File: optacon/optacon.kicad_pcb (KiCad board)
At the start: 2 copper layers, 41.1 x 28.6 mm, 9 parts, among them J1 Conn_01x22, J2 Conn_01x08, J3 Conn_01x02, U1 HV528, U2 HV528

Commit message: schematic, footprints
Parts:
- added C1: 1 µF, Capacitor_SMD:C_0805_2012Metric, F.Cu at (157.4, 88.8)
- added C2: 0.1 µF, Capacitor_SMD:C_0805_2012Metric, F.Cu at (151.7, 92.1)
- added C3: 0.1 µF, Capacitor_SMD:C_0805_2012Metric, F.Cu at (162.9, 82.5)
- added C4: 0.1 µF 150V+, Capacitor_SMD:C_1206_3216Metric, F.Cu at (152.3, 89.0)
- added D1: D, Diode_SMD:D_0805_2012Metric, F.Cu at (91.9, 125.6)
- added L1: 3.3 µH, microchip_hv:TDK_VLS_3012, F.Cu at (158.2, 83.6)
- added R1: 549k, Resistor_SMD:R_0805_2012Metric, F.Cu at (151.7, 95.1)
- added R2: 6.98k, Resistor_SMD:R_0805_2012Metric, F.Cu at (162.9, 85.5)
- added R3: 6.98k, Resistor_SMD:R_0805_2012Metric, F.Cu at (161.8, 88.4)
- added R4: 3.3k, Resistor_SMD:R_0805_2012Metric, F.Cu at (151.7, 98.1)
- added R5: 3.3k, Resistor_SMD:R_0805_2012Metric, F.Cu at (156.2, 92.1)
- added U3: DRV2665, Package_DFN_QFN:Texas_S-PVQFN-N20_EP2.7x2.7mm_ThermalVias, F.Cu at (152.7, 84.1)
- added piezo1: Conn_01x21, microchip_hv:piezox20, F.Cu at (104.0, 83.5)
- J1: value Conn_01x22 -> Conn_01x12; footprint microchip_hv:piezox20 -> microchip_hv:FH34SRJ-12S-0.5SH
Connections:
- J1 pad 1: /reed1 -> /VDD
- J1 pad 10: /reed10 -> /SCL
- J1 pad 11: /reed11 -> /SDA
- J1 pad 12: /reed12 -> /REG
- J1 pad 2: /reed2 -> /VBIAS
- J1 pad 3: /reed3 -> /DIN
- J1 pad 4: /reed4 -> /CLK
- J1 pad 5: /reed5 -> /POL
- J1 pad 6: /reed6 -> /LE
- J1 pad 7: /reed7 -> /DOUT
- J1 pad 8: /reed8 -> GND
- J1 pad 9: /reed9 -> /IN+
- U1 pad 10: /PZT+ -> /PZT_Common
- U1 pad 11: /PZT+ -> /PZT_Common
- U1 pad 12: /PZT+ -> /PZT_Common
- U1 pad 29: /PZT- -> /PZT_Common
- U1 pad 30: /PZT- -> /PZT_Common
- U1 pad 31: /PZT- -> /PZT_Common
- U2 pad 10: /PZT+ -> /PZT_Common
- U2 pad 11: /PZT+ -> /PZT_Common
- U2 pad 12: /PZT+ -> /PZT_Common
- U2 pad 29: /PZT- -> /PZT_Common
- U2 pad 30: /PZT- -> /PZT_Common
- U2 pad 31: /PZT- -> /PZT_Common
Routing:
- net /PZT_Common: track 0.00 -> 116.4 mm, vias 0 -> 28
- net /PZT+: track 66.9 -> 0.00 mm, vias 23 -> 0
- net /PZT-: track 49.5 -> 0.00 mm, vias 5 -> 0
- net /reed11: track 10.1 -> 0.00 mm, vias 1 -> 0
- net /POL: track 19.8 -> 29.9 mm, vias 3 -> 4
- net GND: track 8.66 -> 17.9 mm, vias 3 -> 4
- net /reed10: track 9.23 -> 0.00 mm, vias 1 -> 0
- net /reed9: track 8.81 -> 0.00 mm, vias 1 -> 0
- net /SCL: track 0.00 -> 8.81 mm, vias 0 -> 1
- net /reed13: track 8.60 -> 0.00 mm, vias 1 -> 0
- net /VDD: track 27.5 -> 36.1 mm, vias 2 -> 3
- net /reed12: track 8.16 -> 0.00 mm, vias 1 -> 0
- net /DIN: track 9.28 -> 17.4 mm, vias 0 -> 1
- net /reed8: track 7.96 -> 0.00 mm, vias 1 -> 0
- net /SDA: track 0.00 -> 7.96 mm, vias 0 -> 1

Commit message: bom update
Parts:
- removed J2: Conn_01x08, Connector_PinHeader_2.54mm:PinHeader_1x08_P2.54mm_Vertical
- removed J3: Conn_01x02, Connector_PinHeader_2.54mm:PinHeader_1x02_P2.54mm_Vertical
- removed REF** (x4): MountingHole_2.2mm_M2_ISO7380, MountingHole:MountingHole_2.2mm_M2_ISO7380
- C1, C2, C3: footprint Capacitor_SMD:C_0805_2012Metric -> Capacitor_SMD:C_0603_1608Metric
- D1: footprint Diode_SMD:D_0805_2012Metric -> Diode_SMD:D_SOD-123F
- R1, R2, R3, R4, R5: footprint Resistor_SMD:R_0805_2012Metric -> Resistor_SMD:R_0603_1608Metric
- moved R2 68.5 mm to (98.0, 63.4), turned to -90 degrees
- moved R1 60.9 mm to (99.7, 63.4), turned to -90 degrees
- moved D1 58.1 mm to (98.4, 67.9), turned to 90 degrees
- moved C4 52.6 mm to (103.7, 68.9), turned to 180 degrees
- moved U3 52.4 mm to (104.2, 64.3)
- moved L1 49.1 mm to (113.0, 64.4)
- moved J1 31.7 mm to (103.0, 52.8), turned to 180 degrees
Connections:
- J1 pad 10: /SCL -> /REG
- J1 pad 11: /SDA -> /AIN
- J1 pad 12: /REG -> GND
- J1 pad 8: GND -> /SCL
- J1 pad 9: /IN+ -> /SDA
- U1 pad 1: /reed2 -> /PZT_Common
- U1 pad 10: /PZT_Common -> /reed8
- U1 pad 11: /PZT_Common -> /reed9
- U1 pad 12: /PZT_Common -> /reed10
- U1 pad 2: /reed3 -> /PZT_Common
- U1 pad 3: /reed4 -> /reed1
- U1 pad 32: /reed1 -> /PZT_Common
- U1 pad 4: /reed5 -> /reed2
- U1 pad 5: /reed6 -> /reed3
- U1 pad 6: /reed7 -> /reed4
- U1 pad 7: /reed8 -> /reed5
- U1 pad 8: /reed9 -> /reed6
- U1 pad 9: /reed10 -> /reed7
- U2 pad 1: /reed12 -> /reed15
- U2 pad 2: /reed13 -> /reed16
- U2 pad 29: /PZT_Common -> /reed11
- U2 pad 3: /reed14 -> /reed17
- U2 pad 30: /PZT_Common -> /reed12
- U2 pad 31: /PZT_Common -> /reed13
- U2 pad 32: /reed11 -> /reed14
- U2 pad 4: /reed15 -> /reed18
- U2 pad 5: /reed16 -> /reed19
- U2 pad 6: /reed17 -> /reed20
- U2 pad 7: /reed18 -> /PZT_Common
- U2 pad 8: /reed19 -> /PZT_Common
- U2 pad 9: /reed20 -> /PZT_Common
- U3 pad 17: /IN+ -> /AIN
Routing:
- net /PZT_Common: track 116.4 -> 0.00 mm, vias 28 -> 0
- net /VDD: track 36.1 -> 0.00 mm, vias 3 -> 0
- net /VPP: track 32.4 -> 0.00 mm, vias 2 -> 0
- net /POL: track 29.9 -> 0.00 mm, vias 4 -> 0
- net /VBIAS: track 22.3 -> 0.00 mm, vias 2 -> 0
- net /CLK: track 22.0 -> 0.00 mm, vias 3 -> 0
- net Net-(U1-Pad24): track 20.8 -> 0.00 mm, vias 2 -> 0
- net /LE: track 20.2 -> 0.00 mm, vias 2 -> 0
- net GND: track 17.9 -> 0.00 mm, vias 4 -> 0
- net /DIN: track 17.4 -> 0.00 mm, vias 1 -> 0
- net /reed1: track 9.98 -> 0.00 mm, vias 1 -> 0
- net /reed20: track 9.44 -> 0.00 mm, vias 1 -> 0
- net /SCL: track 8.81 -> 0.00 mm, vias 1 -> 0
- net /reed19: track 8.74 -> 0.00 mm, vias 1 -> 0
- net /reed3: track 8.53 -> 0.00 mm, vias 1 -> 0
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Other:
- board size 41.1 x 28.6 mm -> 124.1 x 73.2 mm
- board text added: "V-SCORE"
- board text removed: "CLK"
- board text removed: "DIN"
- board text removed: "DO"
- board text removed: "GND"
- board text removed: "LE"
- board text removed: "POL"
- board text removed: "VBS"
- board text removed: "VDD"
- board text removed: "VPP"

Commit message: driver board
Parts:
- added C5: 0.1µF, Capacitor_SMD:C_1206_3216Metric, F.Cu at (116.9, 70.9)
- added R6: 0, Resistor_SMD:R_0603_1608Metric, F.Cu at (97.6, 54.3)
- added R7: 0R, Resistor_SMD:R_1206_3216Metric, F.Cu at (120.5, 63.9)
- added R8: DNP, Resistor_SMD:R_1206_3216Metric, F.Cu at (115.4, 63.9)
- L1: value 3.3 µH -> VLS3012HBX-3R3M
- moved R4 71.0 mm to (93.3, 57.8), turned to 180 degrees
- moved R5 70.7 mm to (93.3, 59.7)
- moved C3 67.0 mm to (102.1, 54.3), turned to 180 degrees
- moved C2 62.9 mm to (100.3, 55.9), turned to 180 degrees
- moved R3 62.3 mm to (109.5, 54.7), turned to 90 degrees
- moved C1 60.7 mm to (102.4, 63.0), turned to 90 degrees
- moved J1 13.0 mm to (90.0, 53.4)
- moved C4 10.6 mm to (109.6, 60.1), turned to -90 degrees
- moved D1 9.17 mm to (104.2, 75.0)
- moved L1 7.83 mm to (105.4, 62.8), turned to 90 degrees
- moved U3 6.27 mm to (104.9, 58.1)
- moved R2 3.35 mm to (97.3, 60.1)
- moved R1 2.51 mm to (97.3, 64.1), turned to 90 degrees
- moved U1 0.76 mm to (98.3, 74.0), turned to 45 degrees
- moved U2 0.68 mm to (109.9, 74.0), turned to 135 degrees
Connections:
- net Net-(C4-Pad1) renamed /VBST
- C3 pad 1: /REG -> Net-(C3-Pad1)
- J1 pad 1: /VDD -> GND
- J1 pad 10: /REG -> /SDA
- J1 pad 11: /AIN -> /REG
- J1 pad 12: GND -> /VDD
- J1 pad 3: /DIN -> /DOUT
- J1 pad 4: /CLK -> /LE
- J1 pad 6: /LE -> /CLK
- J1 pad 7: /DOUT -> /DIN
- J1 pad 8: /SCL -> /AIN
- J1 pad 9: /SDA -> /SCL
- U1 pad 17: /DIN -> Net-(U2-Pad24)
- U1 pad 24: Net-(U1-Pad24) -> /DOUT
- U2 pad 17: Net-(U1-Pad24) -> /DIN
- U2 pad 24: /DOUT -> Net-(U2-Pad24)
- U3 pad 13: /VPP -> /VOUT
- U3 pad 16: /hv_driver/IN- -> GND
- U3 pad 20: /REG -> Net-(C3-Pad1)
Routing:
- net /PZT_Common: track 0.00 -> 63.1 mm
- net /VDD: track 0.00 -> 49.9 mm, vias 0 -> 4
- net /CLK: track 0.00 -> 38.3 mm, vias 0 -> 2
- net /POL: track 0.00 -> 38.1 mm, vias 0 -> 2
- net GND: track 0.00 -> 37.9 mm, vias 0 -> 11
- net /VPP: track 0.00 -> 37.3 mm, vias 0 -> 3
- net /VBIAS: track 0.00 -> 34.6 mm, vias 0 -> 2
- net /LE: track 0.00 -> 34.3 mm, vias 0 -> 1
- net /DIN: track 0.00 -> 28.7 mm
- net /VBST: track 0.00 -> 28.5 mm, vias 0 -> 2
- net /SCL: track 0.00 -> 23.0 mm
- net /DOUT: track 0.00 -> 22.0 mm
- net /AIN: track 0.00 -> 20.1 mm
- net /SDA: track 0.00 -> 19.5 mm
- net /VOUT: track 0.00 -> 17.8 mm
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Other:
- board size 124.1 x 73.2 mm -> 61.9 x 78.5 mm
- board text added: "vscore"
- board text removed: "V-SCORE"

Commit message: cleanup
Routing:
- net /LE: vias 1 -> 0
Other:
- board text added: "piezo driver board rev 2"

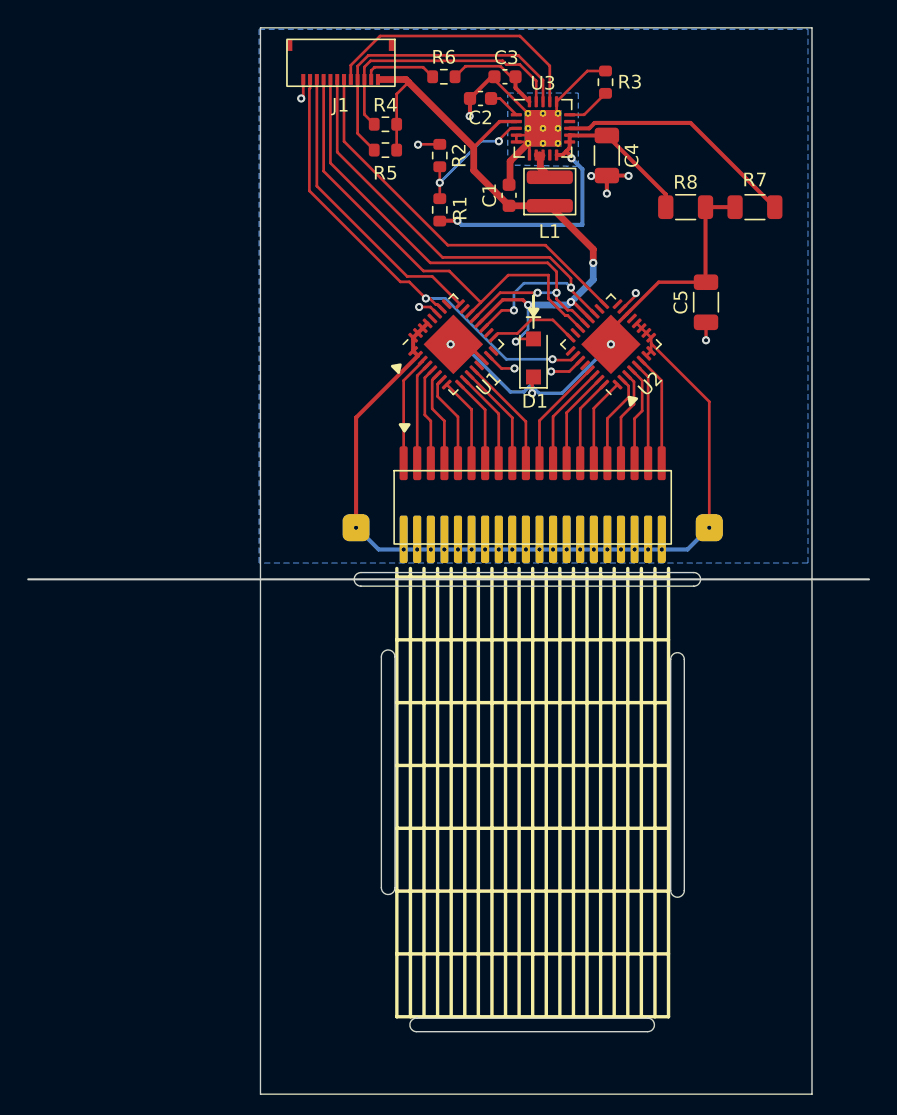
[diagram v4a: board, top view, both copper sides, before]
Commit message: hole pattern for piezo vacuum
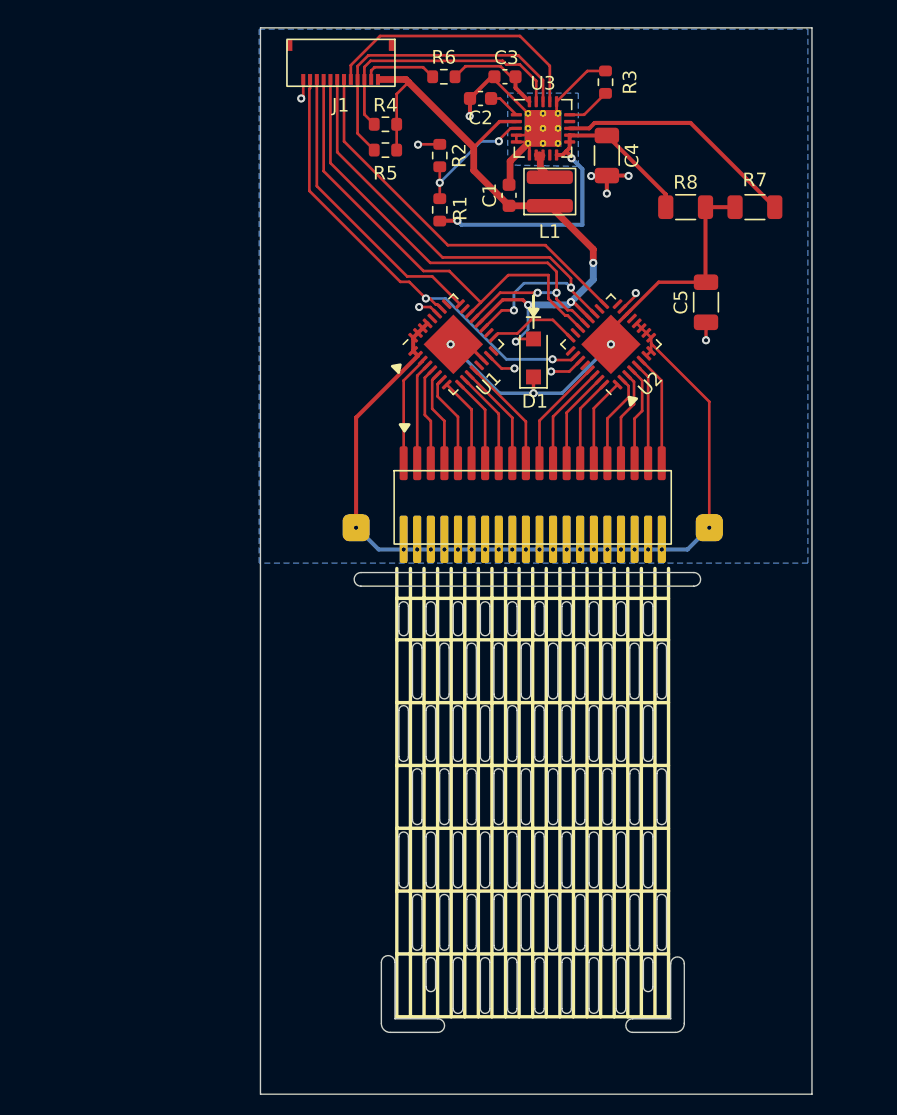
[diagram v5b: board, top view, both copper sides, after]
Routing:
- net /VPP: track 37.3 -> 36.2 mm
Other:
- board size 61.9 x 78.5 mm -> 40.6 x 78.5 mm
- board text added: "DANGER DANGER HIGH VOLTAGE"

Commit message: gerbers
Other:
- board size 40.6 x 78.5 mm -> 61.9 x 78.5 mm
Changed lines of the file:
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@@
     ) (layer "F.SilkS") (width 0.2) (fill solid))
   (gr_line (start 104.2 70.4) (end 104.2 71.9) (layer "F.SilkS") (width 0.15))
-  (gr_line (start 128.9 91.3) (end 67 91.3) (layer "Cmts.User") (width 0.15))
   (gr_rect (start 84.1 50.7) (end 124.7 129.2) (layer "Edge.Cuts") (width 0.1) (fill none))
   (gr_arc (start 114.3 119.6) (mid 114.8 119.1) (end 115.3 119.6) (layer "Edge.Cuts") (width 0.1))
@@
   (gr_arc (start 115.3 124) (mid 115.109619 124.459619) (end 114.65 124.65) (layer "Edge.Cuts") (width 0.1))
   (gr_line (start 111.5 123.65) (end 114.3 123.65) (layer "Edge.Cuts") (width 0.1))
+  (gr_line (start 128.9 91.3) (end 67 91.3) (layer "Edge.Cuts") (width 0.15))
   (gr_line (start 94 119.5) (end 94 123.65) (layer "Edge.Cuts") (width 0.1))
   (gr_line (start 93 119.5) (end 93 124) (layer "Edge.Cuts") (width 0.1))
@@
     (effects (font (size 1 1) (thickness 0.15)) (justify mirror))
   )
-  (gr_text "vscore\n" (at 63.9 91.1) (layer "Cmts.User")
+  (gr_text "vscore\n" (at 63.9 91.1) (layer "Edge.Cuts")
     (effects (font (size 1 1) (thickness 0.15)))
   )

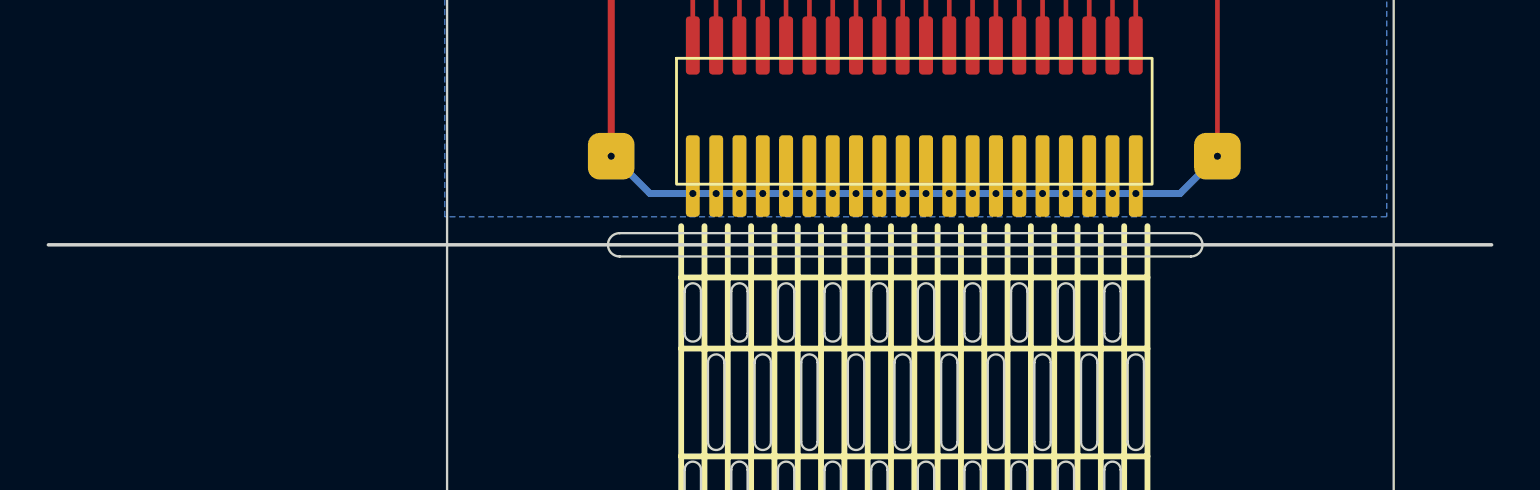
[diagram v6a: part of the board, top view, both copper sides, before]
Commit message: no paste (stencil) for piezo individual pads
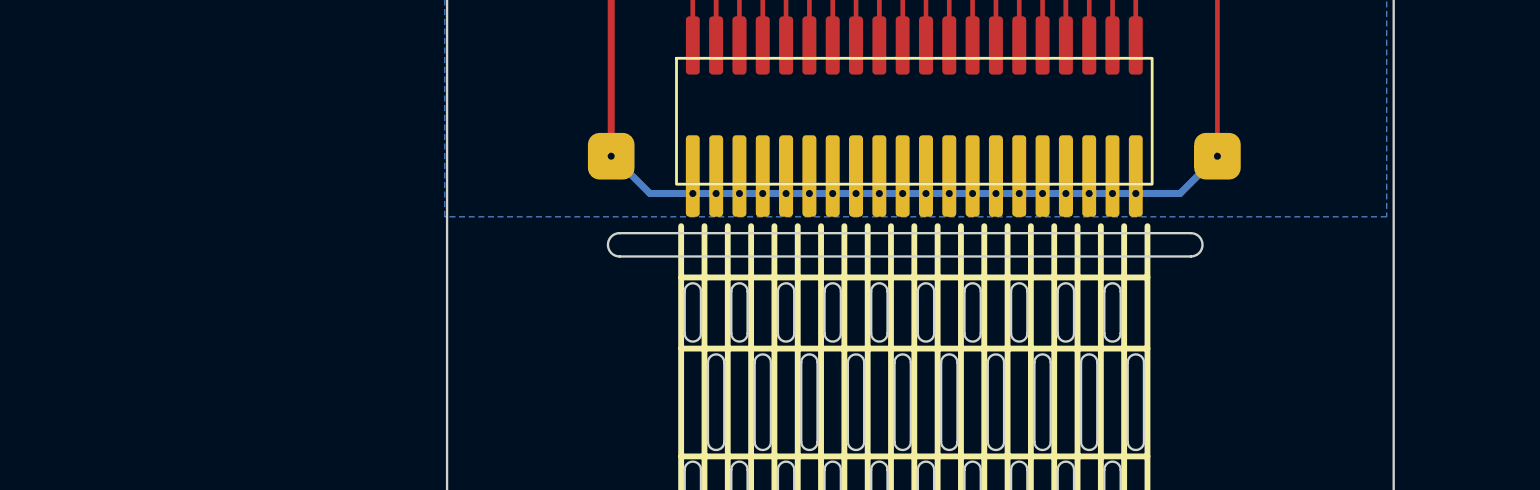
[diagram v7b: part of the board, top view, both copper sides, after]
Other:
- board size 61.9 x 78.5 mm -> 40.6 x 78.5 mm
